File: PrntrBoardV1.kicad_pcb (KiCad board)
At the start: 4 copper layers, 99 x 99 mm, 238 parts, among them J1 EXT 5V, J10 Probe, J11 Extruder Heater, J12 Stepper, J13 Thermistor, J14 Max, J15 Min, J16 Max, J17 Min, J18 Max, J19 Min, J2 Bed Heater, J20 Stepper, J21 Stepper, J22 Stepper, J23 Stepper, J24 Probe, J25 Extruder Heater, J26 Stepper, J27 Thermistor, J28 Thermistor, J29 12-24V, J3 Z Probe, J30 LCD, J31 TC1, J32 TC2, J33 Vin, J34 Vin, J35 5V, J36 5V, J4 E0 Cool, J5 E0 Part, J6 E1 Cool, J7 E1 Part, J8 Always On Fan 1, J9 Always On Fan 2, U1 4078, U11 NUCLEO-64, U2 74HCT02, U3 74LVC125, U4 TMC5130, U5 TMC5130, U6 TMC5130, U7 TMC5130, U8 TMC5130, X1 16MHz

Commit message: Update libraries. Board revision.
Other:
- board text added: "rev 3"
- board text removed: "rev 2"
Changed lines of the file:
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@@
-(kicad_pcb (version 20171130) (host pcbnew 6.0.0-rc1-unknown-0cca1c6~65~ubuntu18.04.1)
+(kicad_pcb (version 20171130) (host pcbnew 6.0.0-rc1-unknown-516cf47~65~ubuntu18.04.1)
   (general
     (thickness 1.6)
@@
     (effects (font (size 1 1) (thickness 0.15)) (justify mirror))
   )
-  (gr_text "rev 2" (at 116.3 32.1 90) (layer B.SilkS)
+  (gr_text "rev 3" (at 116.3 32.1 90) (layer B.SilkS)
     (effects (font (size 1.5 1.5) (thickness 0.3)) (justify mirror))
   )

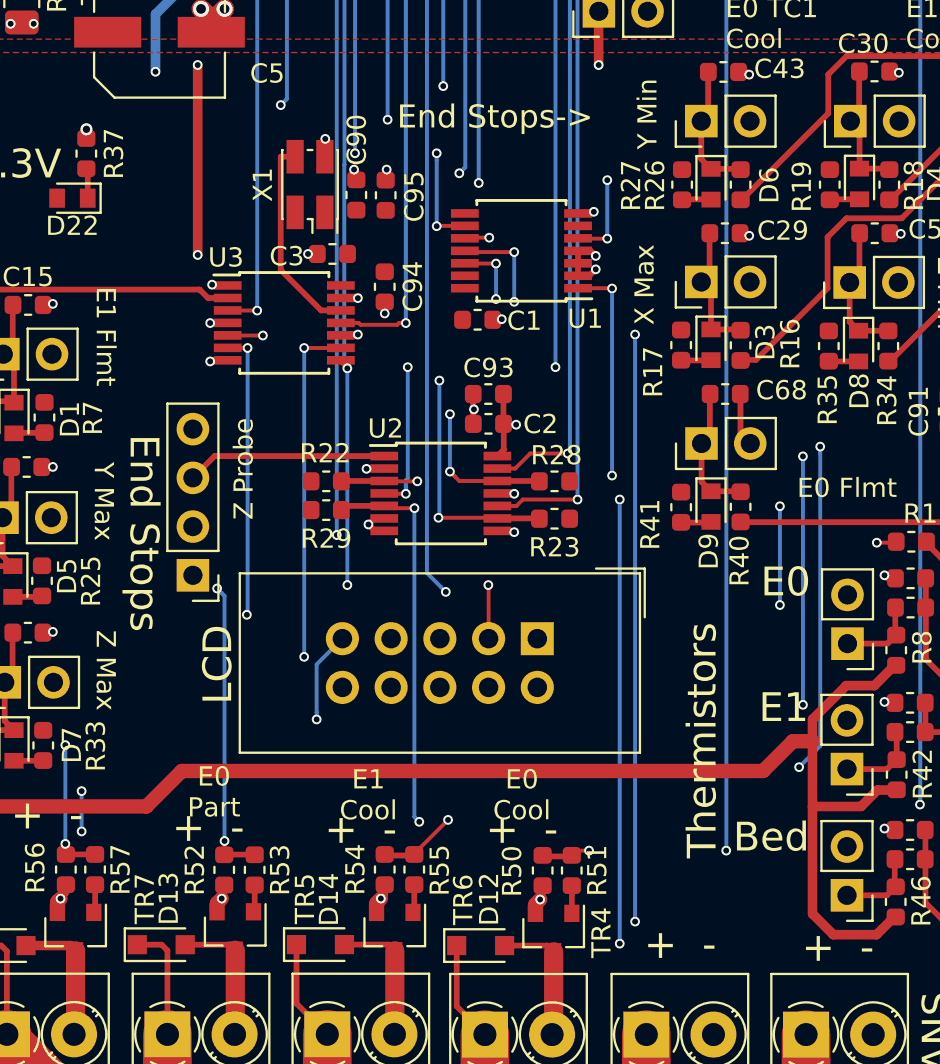
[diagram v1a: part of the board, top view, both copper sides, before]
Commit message: Started rev 3. Added encoder iand button input. Re-routed LCD A0 and RESET to be connected to the HW I2C pins.
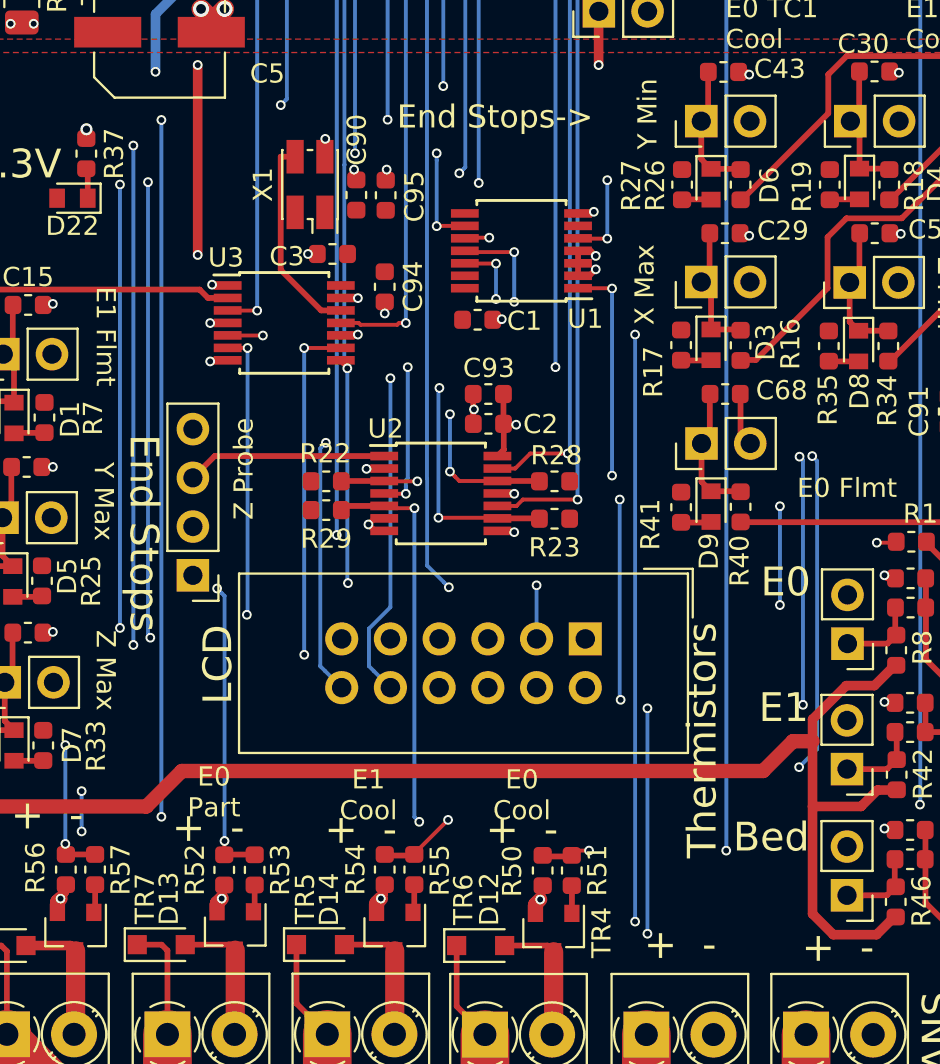
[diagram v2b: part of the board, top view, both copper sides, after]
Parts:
- J30: footprint Connector_IDC:IDC-Header_2x05_P2.54mm_Vertical -> Connector_IDC:IDC-Header_2x06_P2.54mm_Vertical
- R1: value 10k -> 1k
- moved J30 2.50 mm to (63.1, 92.3)
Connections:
- J30 pad 10: GND -> /ENC_A
- J30 pad 8: GND -> /BTN_IN
- U11 pad 13: Net-(U11-Pad13) -> /ENC_A
- U11 pad 15: Net-(U11-Pad15) -> /ENC_B
- U11 pad 25: /LCD_A0 -> /BTN_IN
- U11 pad 27: /~LCD_CS -> /Z_PROBE_MOD
- U11 pad 37: /Z_PROBE_MOD -> /~LCD_CS
- U11 pad 41: /~E0_CS -> /~LCD_RESET
- U11 pad 43: /~E1_CS -> /LCD_A0
- U11 pad 62: /~LCD_RESET -> /~E1_CS
- U11 pad 69: Net-(U11-Pad69) -> /~E0_CS
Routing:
- net /ENC_B: track 0.00 -> 51.7 mm, vias 0 -> 1
- net /ENC_A: track 0.00 -> 51.5 mm, vias 0 -> 1
- net /~E0_CS: track 74.9 -> 110.7 mm, vias 3 -> 5
- net /BTN_IN: track 0.00 -> 32.2 mm
- net /~E1_CS: track 78.2 -> 105.3 mm, vias 3 -> 5
- net /~LCD_RESET: track 31.8 -> 58.9 mm, vias 0 -> 2
- net /LCD_A0: track 32.3 -> 56.6 mm, vias 0 -> 2
- net /Z_PROBE_MOD: track 60.1 -> 48.7 mm
- net /~LCD_CS: track 43.1 -> 49.1 mm, vias 1 -> 2
- net /Z_DIR: track 135.8 -> 138.9 mm
- net /SCK_BUF: track 246.8 -> 249.3 mm

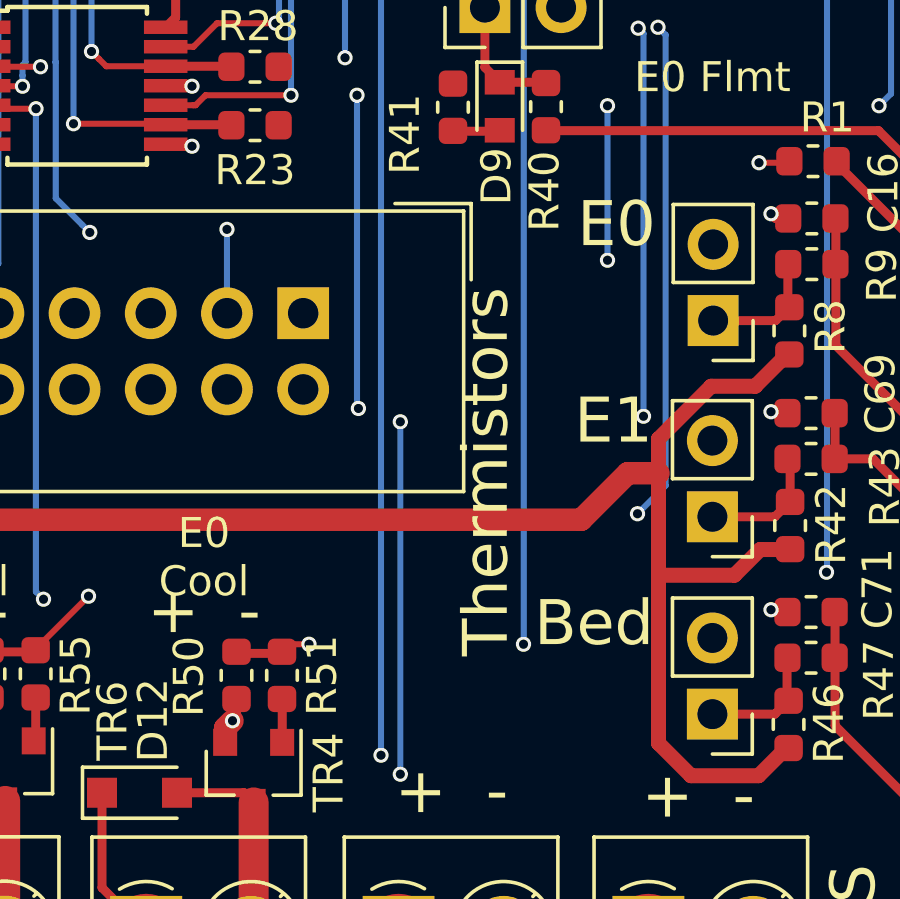
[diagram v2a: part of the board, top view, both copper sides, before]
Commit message: Improve 5V to the LCD.
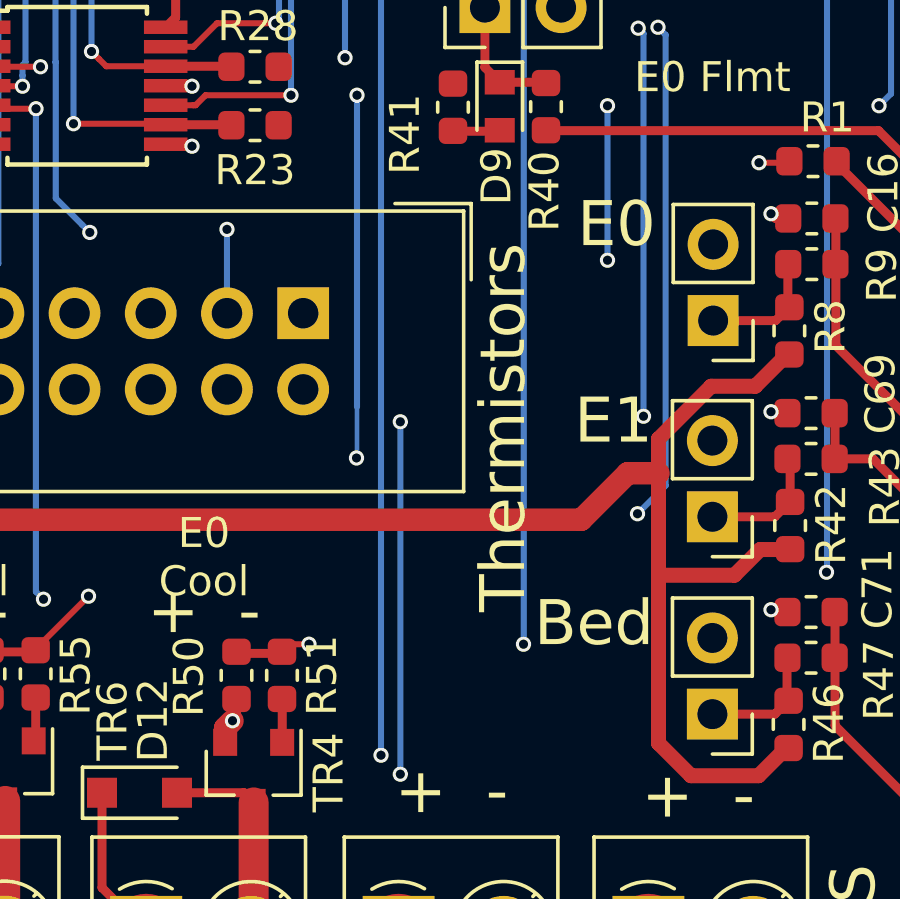
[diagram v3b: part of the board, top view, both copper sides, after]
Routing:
- net /Z_PROBE_MOD: track 48.7 -> 49.3 mm
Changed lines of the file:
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@@
     (thickness 1.6)
     (drawings 133)
-    (tracks 2609)
+    (tracks 2608)
     (zones 0)
     (modules 238)
@@
   )
   (setup
-    (last_trace_width 0.2032)
+    (last_trace_width 0.1524)
     (user_trace_width 0.1524)
     (user_trace_width 0.2032)
@@
     (fp_line (start -0.8 -0.4) (end 0.8 -0.4) (layer F.Fab) (width 0.1))
     (fp_line (start -0.8 0.4) (end -0.8 -0.4) (layer F.Fab) (width 0.1))
-    (pad 2 smd roundrect (at 0.7875 0 135) (size 0.875 0.95) (layers F.Cu F.Paste F.Mask) (roundrect_rratio 0.25)
+    (pad 2 smd roundrect (at 0.787501 0 135) (size 0.875 0.95) (layers F.Cu F.Paste F.Mask) (roundrect_rratio 0.25)
       (net 157 "Net-(C36-Pad2)"))
-    (pad 1 smd roundrect (at -0.7875 0 135) (size 0.875 0.95) (layers F.Cu F.Paste F.Mask) (roundrect_rratio 0.25)
+    (pad 1 smd roundrect (at -0.787501 0 135) (size 0.875 0.95) (layers F.Cu F.Paste F.Mask) (roundrect_rratio 0.25)
       (net 156 "Net-(C36-Pad1)"))
     (model ${KISYS3DMOD}/Capacitor_SMD.3dshapes/C_0603_1608Metric.wrl
@@
     (fp_line (start -0.8 -0.4) (end 0.8 -0.4) (layer F.Fab) (width 0.1))
     (fp_line (start -0.8 0.4) (end -0.8 -0.4) (layer F.Fab) (width 0.1))
-    (pad 2 smd roundrect (at 0.7875 0 315) (size 0.875 0.95) (layers F.Cu F.Paste F.Mask) (roundrect_rratio 0.25)
+    (pad 2 smd roundrect (at 0.787501 0 315) (size 0.875 0.95) (layers F.Cu F.Paste F.Mask) (roundrect_rratio 0.25)
       (net 172 "Net-(C9-Pad2)"))
-    (pad 1 smd roundrect (at -0.7875 0 315) (size 0.875 0.95) (layers F.Cu F.Paste F.Mask) (roundrect_rratio 0.25)
+    (pad 1 smd roundrect (at -0.787501 0 315) (size 0.875 0.95) (layers F.Cu F.Paste F.Mask) (roundrect_rratio 0.25)
       (net 173 "Net-(C9-Pad1)"))
     (model ${KISYS3DMOD}/Capacitor_SMD.3dshapes/C_0603_1608Metric.wrl
@@
     (fp_line (start -0.8 -0.4) (end 0.8 -0.4) (layer F.Fab) (width 0.1))
     (fp_line (start -0.8 0.4) (end -0.8 -0.4) (layer F.Fab) (width 0.1))
-    (pad 2 smd roundrect (at 0.7875 0 135) (size 0.875 0.95) (layers F.Cu F.Paste F.Mask) (roundrect_rratio 0.25)
+    (pad 2 smd roundrect (at 0.787501 0 135) (size 0.875 0.95) (layers F.Cu F.Paste F.Mask) (roundrect_rratio 0.25)
       (net 152 "Net-(C62-Pad2)"))
-    (pad 1 smd roundrect (at -0.7875 0 135) (size 0.875 0.95) (layers F.Cu F.Paste F.Mask) (roundrect_rratio 0.25)
+    (pad 1 smd roundrect (at -0.787501 0 135) (size 0.875 0.95) (layers F.Cu F.Paste F.Mask) (roundrect_rratio 0.25)
       (net 153 "Net-(C62-Pad1)"))
     (model ${KISYS3DMOD}/Capacitor_SMD.3dshapes/C_0603_1608Metric.wrl
@@
     (fp_line (start -0.8 -0.4) (end 0.8 -0.4) (layer F.Fab) (width 0.1))
     (fp_line (start -0.8 0.4) (end -0.8 -0.4) (layer F.Fab) (width 0.1))
-    (pad 2 smd roundrect (at 0.7875 0 225) (size 0.875 0.95) (layers F.Cu F.Paste F.Mask) (roundrect_rratio 0.25)
+    (pad 2 smd roundrect (at 0.787501 0 225) (size 0.875 0.95) (layers F.Cu F.Paste F.Mask) (roundrect_rratio 0.25)
       (net 132 "Net-(C84-Pad2)"))
-    (pad 1 smd roundrect (at -0.7875 0 225) (size 0.875 0.95) (layers F.Cu F.Paste F.Mask) (roundrect_rratio 0.25)
+    (pad 1 smd roundrect (at -0.787501 0 225) (size 0.875 0.95) (layers F.Cu F.Paste F.Mask) (roundrect_rratio 0.25)
       (net 133 "Net-(C84-Pad1)"))
     (model ${KISYS3DMOD}/Capacitor_SMD.3dshapes/C_0603_1608Metric.wrl
@@
     (fp_line (start -0.8 -0.4) (end 0.8 -0.4) (layer F.Fab) (width 0.1))
     (fp_line (start -0.8 0.4) (end -0.8 -0.4) (layer F.Fab) (width 0.1))
-    (pad 2 smd roundrect (at 0.7875 0 135) (size 0.875 0.95) (layers F.Cu F.Paste F.Mask) (roundrect_rratio 0.25)
+    (pad 2 smd roundrect (at 0.787501 0 135) (size 0.875 0.95) (layers F.Cu F.Paste F.Mask) (roundrect_rratio 0.25)
       (net 137 "Net-(C80-Pad2)"))
-    (pad 1 smd roundrect (at -0.7875 0 135) (size 0.875 0.95) (layers F.Cu F.Paste F.Mask) (roundrect_rratio 0.25)
+    (pad 1 smd roundrect (at -0.787501 0 135) (size 0.875 0.95) (layers F.Cu F.Paste F.Mask) (roundrect_rratio 0.25)
       (net 136 "Net-(C80-Pad1)"))
     (model ${KISYS3DMOD}/Capacitor_SMD.3dshapes/C_0603_1608Metric.wrl
@@
     (effects (font (size 1.5 1.5) (thickness 0.3)))
   )
-  (gr_text Thermistors (at 69.15 97.55 90) (layer F.SilkS)
+  (gr_text Thermistors (at 69.723 96.0755 90) (layer F.SilkS)
     (effects (font (size 1.5 1.5) (thickness 0.3)))
   )
@@
   (segment (start 52.589701 84.05) (end 52.573301 84.0336) (width 0.2032) (layer F.Cu) (net 73))
   (segment (start 54.3 84.05) (end 52.589701 84.05) (width 0.2032) (layer F.Cu) (net 73))
-  (via (at 64.897 95.4405) (size 0.508) (drill 0.3048) (layers F.Cu B.Cu) (net 73))
   (segment (start 64.85 85) (end 64.85 95.3935) (width 0.2032) (layer B.Cu) (net 73))
-  (segment (start 64.85 95.3935) (end 64.897 95.4405) (width 0.2032) (layer B.Cu) (net 73))
-  (segment (start 64.897 95.4405) (end 65.532 94.8055) (width 0.2032) (layer In2.Cu) (net 73))
-  (segment (start 80.771818 94.8055) (end 83.432319 97.466001) (width 0.2032) (layer In2.Cu) (net 73))
-  (segment (start 65.532 94.8055) (end 80.771818 94.8055) (width 0.2032) (layer In2.Cu) (net 73))
-  (segment (start 83.432319 97.466001) (end 85.443999 97.466001) (width 0.2032) (layer In2.Cu) (net 73))
-  (segment (start 85.698001 97.211999) (end 86.46 96.45) (width 0.2032) (layer In2.Cu) (net 73))
-  (segment (start 85.443999 97.466001) (end 85.698001 97.211999) (width 0.2032) (layer In2.Cu) (net 73))
+  (via (at 64.8335 97.0915) (size 0.508) (drill 0.3048) (layers F.Cu B.Cu) (net 73))
+  (segment (start 64.85 95.3935) (end 64.85 97.075) (width 0.1524) (layer B.Cu) (net 73))
+  (segment (start 64.85 97.075) (end 64.8335 97.0915) (width 0.1524) (layer B.Cu) (net 73))
+  (segment (start 64.8335 97.0915) (end 65.332401 97.590401) (width 0.1524) (layer In2.Cu) (net 73))
+  (segment (start 85.698001 97.211999) (end 86.46 96.45) (width 0.1524) (layer In2.Cu) (net 73))
+  (segment (start 85.319599 97.590401) (end 85.698001 97.211999) (width 0.1524) (layer In2.Cu) (net 73))
+  (segment (start 65.332401 97.590401) (end 85.319599 97.590401) (width 0.1524) (layer In2.Cu) (net 73))
   (via (at 36.8 102.3) (size 0.508) (drill 0.3048) (layers F.Cu B.Cu) (net 77))
   (segment (start 23.721999 103.308001) (end 22.96 104.07) (width 0.2032) (layer In2.Cu) (net 77))
@@
   (segment (start 107.754599 99.5073) (end 107.860936 99.613637) (width 0.3) (layer F.Cu) (net 77))
   (segment (start 106.704599 99.5073) (end 107.754599 99.5073) (width 0.3) (layer F.Cu) (net 77))
-  (segment (start 83.592796 97.821612) (end 85.591297 97.821612) (width 0.2032) (layer In2.Cu) (net 77))
-  (segment (start 81.258607 100.155801) (end 83.592796 97.821612) (width 0.2032) (layer In2.Cu) (net 77))
-  (segment (start 105.378684 97.367277) (end 107.606937 99.59553) (width 0.2032) (layer In2.Cu) (net 77))
-  (segment (start 107.606937 99.59553) (end 107.860936 99.849529) (width 0.2032) (layer In2.Cu) (net 77))
-  (segment (start 88.15 97.367277) (end 105.378684 97.367277) (width 0.2032) (layer In2.Cu) (net 77))
   (segment (start 87.901476 97.615801) (end 88.15 97.367277) (width 0.2032) (layer In2.Cu) (net 77))
-  (segment (start 85.797108 97.615801) (end 87.901476 97.615801) (width 0.2032) (layer In2.Cu) (net 77))
+  (segment (start 107.606937 99.59553) (end 107.860936 99.849529) (width 0.2032) (layer In2.Cu) (net 77))
   (segment (start 39.8 100.155801) (end 81.258607 100.155801) (width 0.2032) (layer In2.Cu) (net 77))
-  (segment (start 85.591297 97.821612) (end 85.797108 97.615801) (width 0.2032) (layer In2.Cu) (net 77))
+  (segment (start 85.797108 97.615801) (end 87.901476 97.615801) (width 0.2032) (layer In2.Cu) (net 77))
+  (segment (start 105.378684 97.367277) (end 107.606937 99.59553) (width 0.2032) (layer In2.Cu) (net 77))
+  (segment (start 83.493796 97.920612) (end 85.492297 97.920612) (width 0.2032) (layer In2.Cu) (net 77))
+  (segment (start 88.15 97.367277) (end 105.378684 97.367277) (width 0.2032) (layer In2.Cu) (net 77))
+  (segment (start 85.492297 97.920612) (end 85.797108 97.615801) (width 0.2032) (layer In2.Cu) (net 77))
+  (segment (start 81.258607 100.155801) (end 83.493796 97.920612) (width 0.2032) (layer In2.Cu) (net 77))
   (segment (start 104.924321 48.328499) (end 105.221501 48.625679) (width 0.2032) (layer In2.Cu) (net 78))
   (via (at 105.613411 50.6051) (size 0.508) (drill 0.3048) (layers F.Cu B.Cu) (net 78))

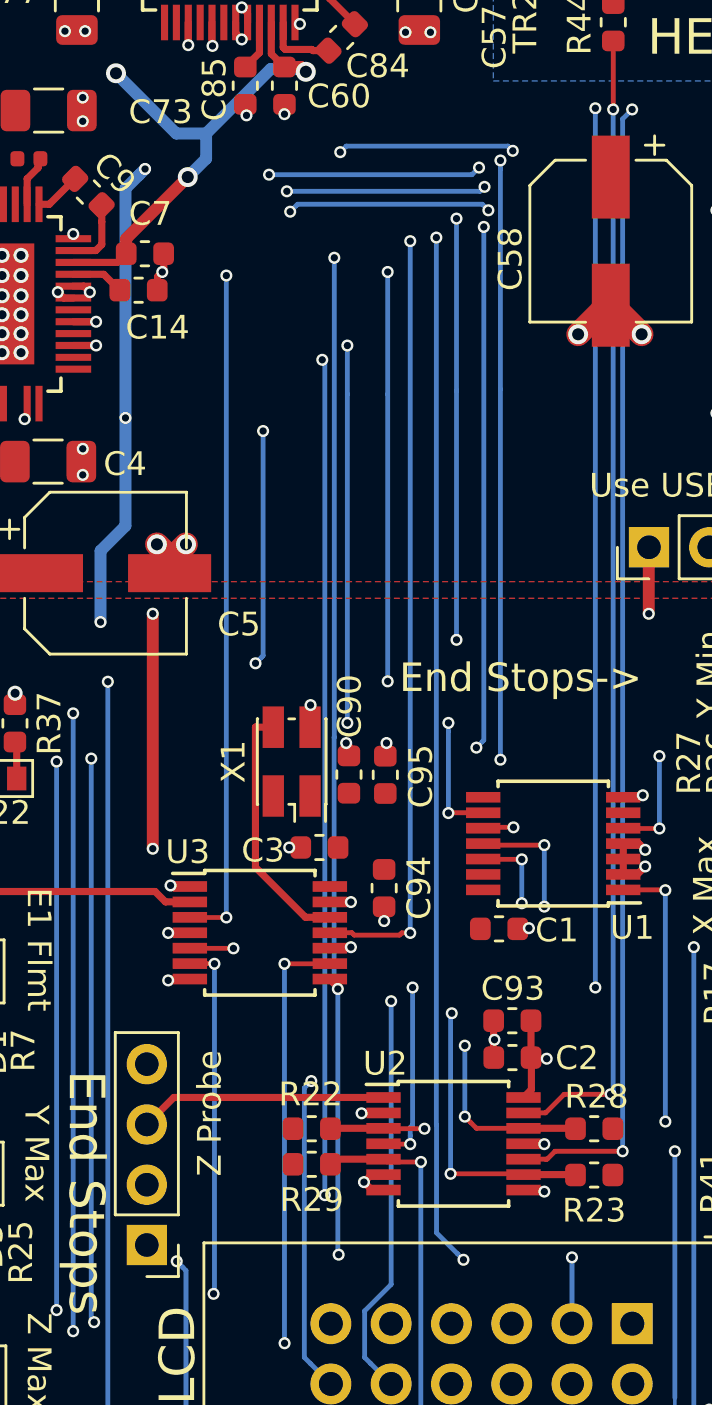
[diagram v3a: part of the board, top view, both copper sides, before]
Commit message: Improve 5V plane.
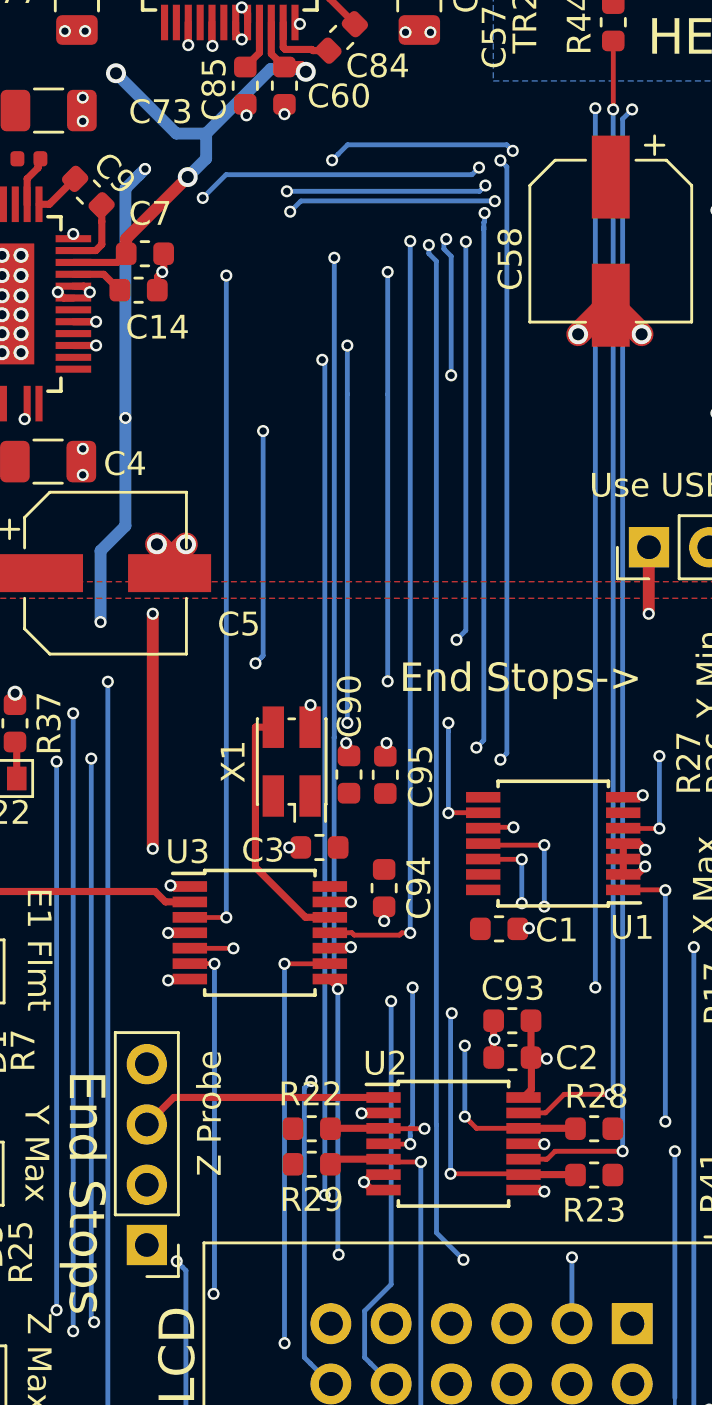
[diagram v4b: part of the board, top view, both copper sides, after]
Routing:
- net /~X_CS: track 85.1 -> 86.4 mm
- net /Z_DIR: track 138.9 -> 140.1 mm
- net /MotorControl/E1_SG: track 51.3 -> 51.8 mm
- net /MISO: vias 13 -> 15
